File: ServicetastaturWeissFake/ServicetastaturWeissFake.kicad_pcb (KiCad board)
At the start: 2 copper layers, 153.7 x 57.2 mm, 72 parts, among them J1 Automat, SW1 Gewinn, SW10 Lautspr./, SW11 ↓0,10, SW12 ↑0,10, SW13 ↓Serie, SW14 ↑Serie, SW15 Zeit, SW16 ↑1,-, SW17 ↙0,10, SW18 ↙1,-, SW19 Auszahlquote, SW2 Foul, SW20 ↙5,-, SW21 Münzsp., SW22 Sp.Zähl, SW23 Lampen, SW24 Reset, SW25 Initialisieren, SW26 Münzung, SW27 Ende, SW28 ↑0,10, SW29 ↓Serie, SW3 ↙2,-, SW30 ↑Serie, SW31 ↓1,-, SW32 ↑1,-, SW4 HW-Test, SW5 Münzsp., SW6 Sp.Zähl, SW7 Dauerlauf, SW8 Reset, SW9 Initialisieren, U1 CC56-12CGKWA, U2 CC56-12CGKWA, U3 74LS48, U4 74LS145, U5 74LS48, U6 74LS145

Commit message: noch eine tastatur
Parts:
- removed D4: LED, LED_SMD:LED_0805_2012Metric
- removed R1, R2, R3, R4, R5, R6, R7, R8, R9: 470 Ω, Resistor_THT:R_Axial_DIN0207_L6.3mm_D2.5mm_P7.62mm_Horizontal
- removed REF**: KiCad-Logo2_6mm_SilkScreen, Symbol:KiCad-Logo2_6mm_SilkScreen
- removed REF**: OSHW-Logo2_9.8x8mm_SilkScreen, Symbol:OSHW-Logo2_9.8x8mm_SilkScreen
- removed REF**: WEEE-Logo_4.2x6mm_SilkScreen, Symbol:WEEE-Logo_4.2x6mm_SilkScreen
- removed REF**: Symbol_CC-ShareAlike_CopperTop_Big, Symbol:Symbol_CC-ShareAlike_CopperTop_Big
- added C5: 1000pF, Capacitor_SMD:C_0603_1608Metric, F.Cu at (159.2, 47.0)
- added C6: 1000pF, Capacitor_SMD:C_0603_1608Metric, F.Cu at (158.0, 36.8)
- added F1: Fuse, Fuse:Fuse_0805_2012Metric, F.Cu at (171.1, 38.1)
- added JP2: Geschwindigkeit, Jumper:SolderJumper-3_P1.3mm_Bridged12_Pad1.0x1.5mm, B.Cu at (167.6, 45.7)
- added R19: 180 kΩ, Resistor_SMD:R_0603_1608Metric, F.Cu at (165.1, 41.5)
- added R20: 180 kΩ, Resistor_SMD:R_0603_1608Metric, F.Cu at (154.5, 35.6)
- added U7: HEF4093B, Package_SO:SOIC-14_3.9x8.7mm_P1.27mm, F.Cu at (158.8, 42.0)
- C3, C4: footprint Capacitor_SMD:C_0805_2012Metric -> Capacitor_SMD:C_0603_1608Metric
- JP1: value Jumper_3_Bridged12 -> Invers; footprint Jumper:SolderJumper-3_P1.3mm_Bridged12_Pad1.0x1.5mm_NumberLabels -> Jumper:SolderJumper-3_P1.3mm_Bridged12_Pad1.0x1.5mm
- R10, R11, R12, R13, R14, R15, R16, R17, R18: footprint Resistor_SMD:R_0805_2012Metric -> Resistor_SMD:R_0603_1608Metric
- U3: value 74LS48 -> 74LS08; footprint Package_DIP:DIP-16_W7.62mm -> Package_SO:SOIC-14_3.9x8.7mm_P1.27mm
- U4: value 74LS145 -> 4017; footprint Package_DIP:DIP-16_W7.62mm -> Package_SO:SOP-16_3.9x9.9mm_P1.27mm
- moved D3 20.2 mm to (137.2, 50.8)
- moved U4 20.2 mm to (159.4, 52.0), turned to 90 degrees
- moved U6 19.7 mm to (147.3, 49.5)
- moved R17 19.3 mm to (138.0, 27.9)
- moved R18 16.3 mm to (138.0, 43.2)
- moved U3 15.4 mm to (158.8, 30.5), turned to 90 degrees
- moved H2 14.3 mm to (172.7, 88.9)
- moved JP1 13.3 mm to (152.4, 41.9)
- moved C2 12.8 mm to (141.0, 45.7), turned to 180 degrees
- moved D1 8.54 mm to (167.6, 78.7)
- moved D2 7.80 mm to (167.6, 61.0)
- moved SW10 7.35 mm to (133.4, 78.8)
- moved SW9 7.35 mm to (151.2, 78.8)
- moved SW11 7.35 mm to (115.7, 78.8)
- moved SW12 7.35 mm to (97.9, 78.8)
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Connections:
- J1 pad 2: +5V -> Net-(J1-Pin_2)
- JP1 pad 3: +5V -> Net-(JP1-B)
- R10 pad 1: Net-(U3-a) -> Net-(U5-a)
- R11 pad 1: Net-(U3-b) -> Net-(U5-b)
- R12 pad 1: Net-(U3-c) -> Net-(U5-c)
- R13 pad 1: Net-(U3-d) -> Net-(U5-d)
- R14 pad 1: Net-(U3-e) -> Net-(U5-e)
- R15 pad 1: Net-(U3-f) -> Net-(U5-f)
- R16 pad 1: Net-(U3-g) -> Net-(U5-g)
- R17 pad 1: +5V -> Net-(R17-Pad1)
- R17 pad 2: unconnected-(R17-Pad2) -> Net-(U1-DPX)
- U3 pad 10: Net-(U3-d) -> Net-(U3-Pad10)
- U3 pad 11: Net-(U3-c) -> unconnected-(U3-Pad11)
- U3 pad 12: Net-(U3-b) -> unconnected-(U3-Pad12)
- U3 pad 13: Net-(U3-a) -> unconnected-(U3-Pad13)
- U3 pad 14: Net-(U3-g) -> +5V
- U3 pad 2: /A2 -> Net-(U3-Pad2)
- U3 pad 3: +5V -> Net-(U3-Pad10)
- U3 pad 4: Net-(JP1-C) -> /A2
- U3 pad 5: +5V -> /A0
- U3 pad 6: /A3 -> Net-(U3-Pad2)
- U3 pad 7: /A0 -> GND
- U3 pad 8: GND -> Net-(R17-Pad1)
- U3 pad 9: Net-(U3-e) -> /A3
- U4 pad 1: Net-(U2-CC4) -> LED5
- U4 pad 10: Net-(JP1-A) -> LED4
- U4 pad 11: Net-(JP1-A) -> LED9
- U4 pad 12: /S3 -> unconnected-(U4-Cout-Pad12)
- U4 pad 13: /S2 -> GND
- U4 pad 14: /S1 -> Net-(JP2-C)
- U4 pad 15: /S0 -> GND
- U4 pad 2: Net-(U2-CC3) -> LED1
- U4 pad 3: Net-(U2-CC2) -> LED0
- U4 pad 4: Net-(U2-CC1) -> LED2
- U4 pad 5: Net-(U1-CC4) -> LED6
- U4 pad 6: Net-(U1-CC3) -> LED7
- U4 pad 7: Net-(U1-CC2) -> LED3
- U4 pad 9: Net-(U1-CC1) -> LED8
- U5 pad 10: Net-(U3-d) -> Net-(U5-d)
- U5 pad 11: Net-(U3-c) -> Net-(U5-c)
- U5 pad 12: Net-(U3-b) -> Net-(U5-b)
- U5 pad 13: Net-(U3-a) -> Net-(U5-a)
- U5 pad 14: Net-(U3-g) -> Net-(U5-g)
- U5 pad 15: Net-(U3-f) -> Net-(U5-f)
- U5 pad 9: Net-(U3-e) -> Net-(U5-e)
- U6 pad 10: Net-(JP1-A) -> unconnected-(U6-Q8-Pad10)
- U6 pad 11: Net-(JP1-A) -> unconnected-(U6-Q9-Pad11)
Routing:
- net /TS7: track 181.9 -> 0.00 mm
- net Net-(U1-CC1): track 165.7 -> 0.00 mm
- net /TS6: track 164.5 -> 0.00 mm
- net Net-(U1-CC2): track 161.0 -> 0.00 mm
- net Net-(U1-CC3): track 159.6 -> 0.00 mm
- net Net-(D2-K): track 151.4 -> 0.00 mm
- net Net-(U1-CC4): track 149.4 -> 0.00 mm
- net /TS5: track 147.2 -> 0.00 mm
- net Net-(D1-K): track 140.9 -> 0.00 mm
- net /TS4: track 129.9 -> 0.00 mm
- net Net-(U1-e): track 117.5 -> 0.00 mm, vias 1 -> 0
- net /TS3: track 112.6 -> 0.00 mm
- net GND: track 111.9 -> 0.00 mm, vias 84 -> 0
- net Net-(U1-d): track 103.6 -> 0.00 mm, vias 1 -> 0
- net +5V: track 100.8 -> 0.00 mm, vias 1 -> 0
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- removed copper zone on B.Cu, net GND
- removed copper zone on F.Cu, net GND
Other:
- board size 153.7 x 57.2 mm -> 154.9 x 68.6 mm
- board text removed: "Die Produkt ionsdaten gibt es gratis online,"
- board text removed: "Materialwert unter 10€"

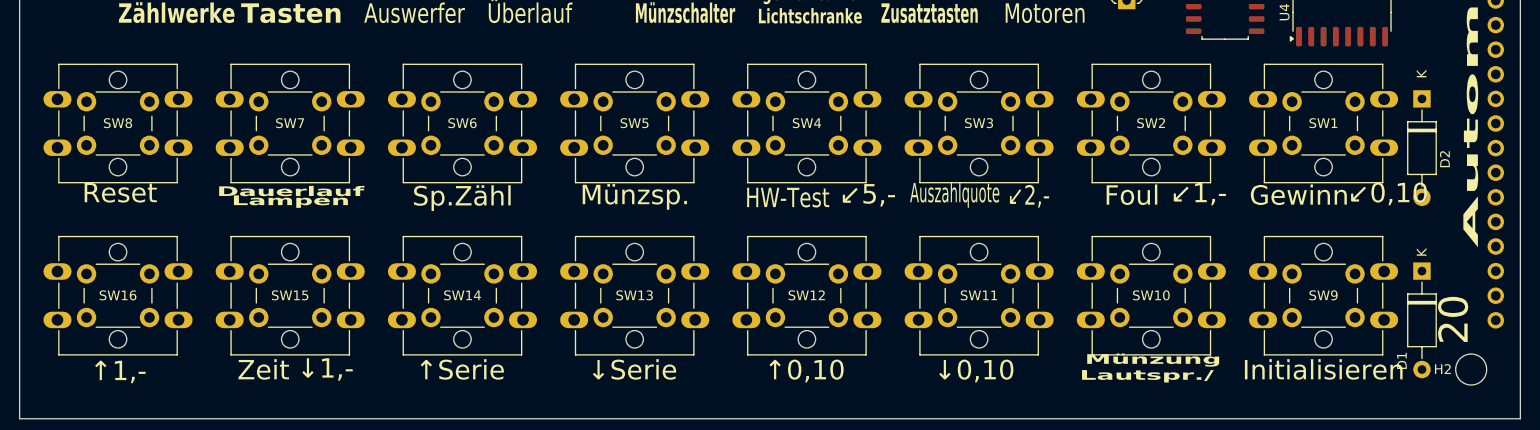
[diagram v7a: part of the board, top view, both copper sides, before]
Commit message: more buttons
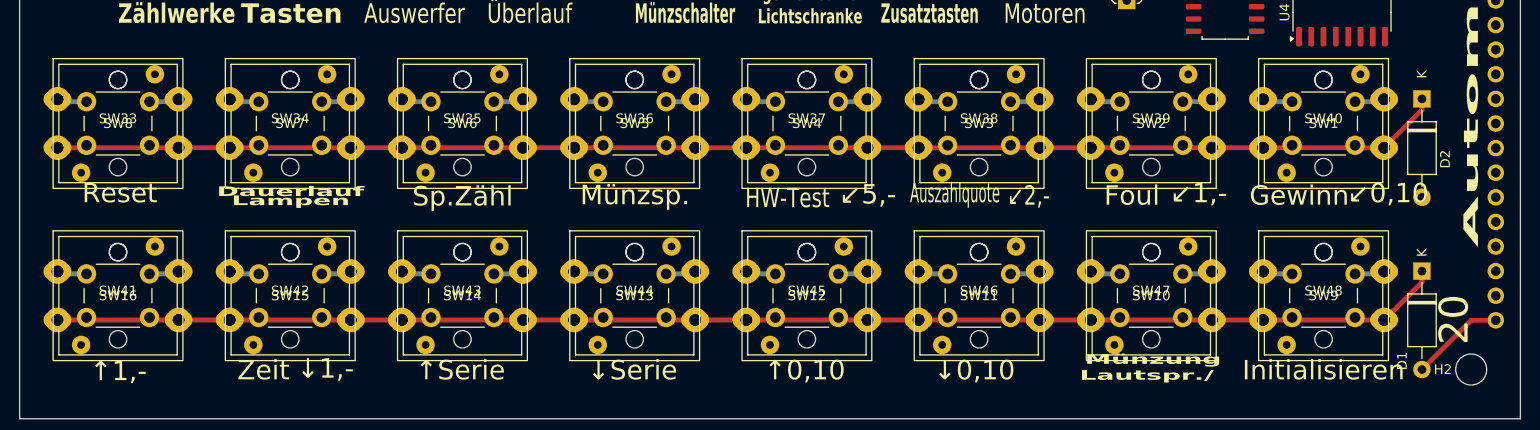
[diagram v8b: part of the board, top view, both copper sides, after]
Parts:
- added SW33: SW_Push_LED, ChinaButton:TS12, F.Cu at (33.0, 63.5)
- added SW34: SW_Push_LED, ChinaButton:TS12, F.Cu at (50.8, 63.5)
- added SW35: SW_Push_LED, ChinaButton:TS12, F.Cu at (68.6, 63.5)
- added SW36: SW_Push_LED, ChinaButton:TS12, F.Cu at (86.4, 63.5)
- added SW37: SW_Push_LED, ChinaButton:TS12, F.Cu at (104.1, 63.5)
- added SW38: SW_Push_LED, ChinaButton:TS12, F.Cu at (121.9, 63.5)
- added SW39: SW_Push_LED, ChinaButton:TS12, F.Cu at (139.7, 63.5)
- added SW40: SW_Push_LED, ChinaButton:TS12, F.Cu at (157.5, 63.5)
- added SW41: SW_Push_LED, ChinaButton:TS12, F.Cu at (33.0, 81.3)
- added SW42: SW_Push_LED, ChinaButton:TS12, F.Cu at (50.8, 81.3)
- added SW43: SW_Push_LED, ChinaButton:TS12, F.Cu at (68.6, 81.3)
- added SW44: SW_Push_LED, ChinaButton:TS12, F.Cu at (86.4, 81.3)
- added SW45: SW_Push_LED, ChinaButton:TS12, F.Cu at (104.1, 81.3)
- added SW46: SW_Push_LED, ChinaButton:TS12, F.Cu at (121.9, 81.3)
- added SW47: SW_Push_LED, ChinaButton:TS12, F.Cu at (139.7, 81.3)
- added SW48: SW_Push_LED, ChinaButton:TS12, F.Cu at (157.5, 81.3)
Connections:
- SW1 pad 1: Net-(D2-K) -> /TS0
- SW1 pad 2: /TS0 -> Net-(D2-K)
- SW10 pad 1: Net-(D1-K) -> /TS1
- SW10 pad 2: /TS1 -> Net-(D1-K)
- SW11 pad 1: Net-(D1-K) -> /TS2
- SW11 pad 2: /TS2 -> Net-(D1-K)
- SW12 pad 1: Net-(D1-K) -> /TS3
- SW12 pad 2: /TS3 -> Net-(D1-K)
- SW13 pad 1: Net-(D1-K) -> /TS4
- SW13 pad 2: /TS4 -> Net-(D1-K)
- SW14 pad 1: Net-(D1-K) -> /TS5
- SW14 pad 2: /TS5 -> Net-(D1-K)
- SW15 pad 1: Net-(D1-K) -> /TS6
- SW15 pad 2: /TS6 -> Net-(D1-K)
- SW16 pad 1: Net-(D1-K) -> /TS7
- SW16 pad 2: /TS7 -> Net-(D1-K)
- SW17 pad 1: Net-(D2-K) -> /TS0
- SW17 pad 2: /TS0 -> Net-(D2-K)
- SW18 pad 1: Net-(D2-K) -> /TS1
- SW18 pad 2: /TS1 -> Net-(D2-K)
- SW19 pad 1: Net-(D2-K) -> /TS2
- SW19 pad 2: /TS2 -> Net-(D2-K)
- SW2 pad 1: Net-(D2-K) -> /TS1
- SW2 pad 2: /TS1 -> Net-(D2-K)
- SW20 pad 1: Net-(D2-K) -> /TS3
- SW20 pad 2: /TS3 -> Net-(D2-K)
- SW21 pad 1: Net-(D2-K) -> /TS4
- SW21 pad 2: /TS4 -> Net-(D2-K)
- SW22 pad 1: Net-(D2-K) -> /TS5
- SW22 pad 2: /TS5 -> Net-(D2-K)
- SW23 pad 1: Net-(D2-K) -> /TS6
- SW23 pad 2: /TS6 -> Net-(D2-K)
- SW24 pad 1: Net-(D2-K) -> /TS7
- SW24 pad 2: /TS7 -> Net-(D2-K)
- SW25 pad 1: Net-(D1-K) -> /TS0
- SW25 pad 2: /TS0 -> Net-(D1-K)
- SW26 pad 1: Net-(D1-K) -> /TS1
- SW26 pad 2: /TS1 -> Net-(D1-K)
- SW27 pad 1: Net-(D1-K) -> /TS2
- SW27 pad 2: /TS2 -> Net-(D1-K)
- SW28 pad 1: Net-(D1-K) -> /TS3
- SW28 pad 2: /TS3 -> Net-(D1-K)
- SW29 pad 1: Net-(D1-K) -> /TS4
- SW29 pad 2: /TS4 -> Net-(D1-K)
- SW3 pad 1: Net-(D2-K) -> /TS2
- SW3 pad 2: /TS2 -> Net-(D2-K)
- SW30 pad 1: Net-(D1-K) -> /TS5
- SW30 pad 2: /TS5 -> Net-(D1-K)
- SW31 pad 1: Net-(D1-K) -> /TS6
- SW31 pad 2: /TS6 -> Net-(D1-K)
- SW32 pad 1: Net-(D1-K) -> /TS7
- SW32 pad 2: /TS7 -> Net-(D1-K)
- SW4 pad 1: Net-(D2-K) -> /TS3
- SW4 pad 2: /TS3 -> Net-(D2-K)
- SW5 pad 1: Net-(D2-K) -> /TS4
- SW5 pad 2: /TS4 -> Net-(D2-K)
- SW6 pad 1: Net-(D2-K) -> /TS5
- SW6 pad 2: /TS5 -> Net-(D2-K)
- SW7 pad 1: Net-(D2-K) -> /TS6
- SW7 pad 2: /TS6 -> Net-(D2-K)
- SW8 pad 1: Net-(D2-K) -> /TS7
- SW8 pad 2: /TS7 -> Net-(D2-K)
- SW9 pad 1: Net-(D1-K) -> /TS0
- SW9 pad 2: /TS0 -> Net-(D1-K)
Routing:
- net Net-(D2-K): track 0.00 -> 143.6 mm
- net Net-(D1-K): track 0.00 -> 143.6 mm
- net /TS4: track 0.00 -> 12.4 mm
- net /TS3: track 0.00 -> 12.4 mm
- net /TS7: track 0.00 -> 12.4 mm
- net /TS6: track 0.00 -> 12.4 mm
- net /TS1: track 0.00 -> 12.4 mm
- net /TS5: track 0.00 -> 12.4 mm
- net /TS0: track 0.00 -> 12.4 mm
- net /TS2: track 0.00 -> 12.4 mm
- net /TZ7: track 0.00 -> 9.72 mm
